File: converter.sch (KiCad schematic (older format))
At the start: 15 parts

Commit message: Schematic mostly complete
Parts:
- removed U?: MSP430G2553-20, ~, symbol MSP430G2553-20
- added C? (x3): CP1, ~, symbol CP1
- added C? (x4): C, ~, symbol C
- added D? (x2): DIODE, ~, symbol DIODE
- added J?: USB-FOO, ~, symbol USB-FOO
- added L?: INDUCTOR, ~, symbol INDUCTOR
- added P? (x11): CONN_1, ~, symbol CONN_1
- added Q?: SOMETHING, SOT-23, symbol BSS138
- added Q? (x2): BC817-40, SOT-23, symbol BC817-40
- added R?: 0.47, ~, symbol R
- added R? (x4): R, ~, symbol R
- added R? (x2): 22, ~, symbol R
- added U?: LT1117-5.0, LLC-20, symbol LM117E
- added U?: MCP6002, symbol MCP6002
- added U?: ATMEGA8U2, symbol ATMEGA8U2
- added X?: CRYSTAL, ~, symbol CRYSTAL
- L?: value INDUCTOR -> 68µH
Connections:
- net labels added: FB_Back, PWM_Back, onewire, xtal1, xtal2
- wire segments 33 -> 108
- no-connect marks 0 -> 1
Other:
- note added: "Back light (3W red)"
- note added: "Front light (15W white)\n"
- note added: "Logic power supply"
- moved on the sheet: C?, D?, L?, P?, R?, U?, U?A

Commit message: First draft PCB layout
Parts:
- removed C?: CP1, ~, symbol CP1
- added C12: 1µ, ~, symbol C
- added C6: 100n, ~, symbol C
- added P7: 12V+, ~, symbol CONN_1
- added P8: 12V-, ~, symbol CONN_1
- added R?: 47k, ~, symbol R
- C1: renamed from C?; value C -> 100n
- C2, C8: renamed from C?; value CP1 -> 100µ
- C3, C5: renamed from C?; value C -> 22p
- C4: renamed from C?; value C -> 1µ
- C7: renamed from C?; value CP1 -> 470µ
- C9: renamed from C?; value CP1 -> 47µ
- D1: renamed from D?; value DIODE -> 1N4148
- P1: renamed from P?; value CONN_1 -> OW1_5V
- P10: renamed from P?; value CONN_1 -> OW3
- P11: renamed from P?; value CONN_1 -> OW3_GND
- P12: renamed from P?; value CONN_1 -> Front+
- P13: renamed from P?; value CONN_1 -> Back+
- P14: renamed from P?; value CONN_1 -> Front-
- P15: renamed from P?; value CONN_1 -> Back-
- P2: renamed from P?; value CONN_1 -> OW1
- P3: renamed from P?; value CONN_1 -> OW1_GND
- P4: renamed from P?; value CONN_1 -> OW2_5V
- P5: renamed from P?; value CONN_1 -> OW2
- P6: renamed from P?; value CONN_1 -> OW2_GND
- P9: renamed from P?; value CONN_1 -> OW3_5V
- R3: renamed from R?; value R -> 4k7
- X1: renamed from X?; value CRYSTAL -> 16MHz
- gave numbers to parts that had none: 24
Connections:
- net labels added: back_neg, back_pos, front_neg, front_pos
- wire segments 108 -> 138

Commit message: Improved ground routing, fixed one error
The error was a missing VCC connection at the back converter's input
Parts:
- removed U2: LT1117-5.0, LLC-20, symbol LM117E
- added U?: LM1117E, LLC-20, symbol LM1117E
- gave numbers to parts that had none: 1
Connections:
- wire segments 138 -> 117
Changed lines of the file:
@@
 LIBS:c_locc-ctrl-cache
 LIBS:usb-mods
+LIBS:lm1117e
 LIBS:converter-cache
 EELAYER 27 0
@@
 Sheet 1 1
 Title ""
-Date "18 oct 2013"
+Date "19 oct 2013"
 Rev ""
 Comp ""
@@
 Text Label 5100 3650 0    60   ~ 0
 PWM_Back
-$Comp
-L LM117E U2
-U 1 1 525F0E52
-P 4150 1100
-F 0 "U2" H 3950 1300 40  0000 C CNN
-F 1 "LT1117-5.0" H 4150 1300 40  0000 L CNN
-F 2 "LLC-20" H 4150 1200 30  0000 C CIN
-F 3 "~" H 4150 1100 60  0000 C CNN
-	1    4150 1100
-	1    0    0    -1
-$EndComp
 $Comp
 L CP1 C2
@@
 	7800 2700 7800 2450
 Wire Wire Line
-	7100 1800 7200 1800
-Wire Wire Line
-	7200 1800 7300 1800
-Wire Wire Line
-	7700 1800 7800 1800
-Wire Wire Line
-	7800 1800 7900 1800
+	7100 1800 7300 1800
+Wire Wire Line
+	7700 1800 7900 1800
 Wire Wire Line
 	7800 2050 7800 1800
@@
 	9300 2100 9350 2100
 Wire Wire Line
-	9850 2200 9900 2200
-Wire Wire Line
-	9900 2200 9950 2200
+	9850 2200 9950 2200
 Connection ~ 9900 2200
 Wire Wire Line
 	10500 2700 10500 2650
 Wire Wire Line
-	10450 2200 10500 2200
-Wire Wire Line
-	10500 2200 10900 2200
+	10450 2200 10900 2200
 Wire Wire Line
 	10500 2200 10500 2250
@@
 Connection ~ 9000 -50
 Wire Wire Line
-	3650 950  3650 1050
-Wire Wire Line
-	3650 1050 3650 1150
+	3650 950  3650 1150
 Wire Wire Line
 	3650 1050 3750 1050
@@
 	4550 1050 4650 1050
 Wire Wire Line
-	4650 950  4650 1050
-Wire Wire Line
-	4650 1050 4650 1150
+	4650 950  4650 1150
 Connection ~ 4650 1050
 Wire Wire Line
@@
 	9300 3750 9350 3750
 Wire Wire Line
-	9850 3850 9900 3850
-Wire Wire Line
-	9900 3850 9950 3850
+	9850 3850 9950 3850
 Connection ~ 9900 3850
 Wire Wire Line
 	10500 4350 10500 4300
 Wire Wire Line
-	10450 3850 10500 3850
-Wire Wire Line
-	10500 3850 10900 3850
+	10450 3850 10900 3850
 Wire Wire Line
 	10500 3850 10500 3900
@@
 	8650 4150 8750 4150
 Wire Wire Line
-	6300 4150 6350 4150
-Wire Wire Line
-	6350 4150 6750 4150
+	6300 4150 6750 4150
 Wire Wire Line
 	6750 4150 6750 3750
 Connection ~ 6350 4150
 Wire Wire Line
-	5900 3450 6350 3450
-Wire Wire Line
-	6350 3450 6500 3450
+	5900 3450 6500 3450
 Wire Wire Line
 	6350 3750 6350 3450
 Connection ~ 6350 3450
 Wire Wire Line
-	5900 3950 5900 4150
-Wire Wire Line
-	5900 4150 5900 4250
+	5900 3950 5900 4250
 Wire Wire Line
 	5900 3950 6050 3950
@@
 	5900 4750 5900 4650
 Wire Wire Line
-	6900 3450 7000 3450
-Wire Wire Line
-	7000 3450 7100 3450
+	6900 3450 7100 3450
 Wire Wire Line
 	7800 4350 7800 4100
 Wire Wire Line
-	7700 3450 7800 3450
-Wire Wire Line
-	7800 3450 7900 3450
+	7700 3450 7900 3450
 Wire Wire Line
 	7800 3450 7800 3700
@@
 	9300 4200 9350 4200
 Wire Wire Line
-	9300 3950 9300 4150
-Wire Wire Line
-	9300 4150 9300 4200
+	9300 3950 9300 4200
 Wire Wire Line
 	9300 3950 9350 3950
@@
 	9300 2550 9350 2550
 Wire Wire Line
-	9300 2300 9300 2500
-Wire Wire Line
-	9300 2500 9300 2550
+	9300 2300 9300 2550
 Wire Wire Line
 	9300 2300 9350 2300
@@
 	2300 1700 2300 1800
 Wire Wire Line
-	2200 1800 2300 1800
-Wire Wire Line
-	2300 1800 2400 1800
+	2200 1800 2400 1800
 Wire Wire Line
 	4250 3300 4250 3250
@@
 	4200 2700 4600 2700
 Wire Wire Line
-	4550 2900 4550 3000
-Wire Wire Line
-	4550 3000 4550 3100
-Wire Wire Line
-	4550 3100 4550 3300
+	4550 2900 4550 3300
 Wire Wire Line
 	4550 2900 4600 2900
@@
 	3850 3050 3600 3050
 Wire Wire Line
-	3900 4100 3900 4350
-Wire Wire Line
-	3900 4350 3900 4400
+	3900 4100 3900 4400
 Connection ~ 3900 4350
 Wire Wire Line
-	4500 4100 4500 4350
-Wire Wire Line
-	4500 4350 4500 4400
+	4500 4100 4500 4400
 Connection ~ 4500 4350
 Wire Wire Line
@@
 	2300 4700 2300 4600
 Wire Wire Line
-	2250 4600 2300 4600
-Wire Wire Line
-	2300 4600 2350 4600
+	2250 4600 2350 4600
 Connection ~ 2300 1800
 Connection ~ 2300 4600
@@
 	9600 2400 9600 2300
 $Comp
-L R R?
+L R R12
 U 1 1 5261574C
 P 5500 3950
-F 0 "R?" V 5580 3950 40  0000 C CNN
+F 0 "R12" V 5580 3950 40  0000 C CNN
 F 1 "47k" V 5507 3951 40  0000 C CNN
 F 2 "~" V 5430 3950 30  0000 C CNN
@@
 Wire Wire Line
 	5500 4450 5600 4450
+$Comp
+L +12V #PWR037
+U 1 1 526283B4
+P 6350 3450
+F 0 "#PWR037" H 6350 3400 20  0001 C CNN
+F 1 "+12V" H 6350 3550 30  0000 C CNN
+F 2 "" H 6350 3450 60  0000 C CNN
+F 3 "" H 6350 3450 60  0000 C CNN
+	1    6350 3450
+	1    0    0    -1
+$EndComp
+$Comp
+L LM1117E U?
+U 1 1 52628562
+P 4150 1100
+F 0 "U?" H 3950 1300 40  0000 C CNN
+F 1 "LM1117E" H 4150 1300 40  0000 L CNN
+F 2 "LLC-20" H 4150 1200 30  0000 C CIN
+F 3 "~" H 4150 1100 60  0000 C CNN
+	1    4150 1100
+	1    0    0    -1
+$EndComp
 $EndSCHEMATC

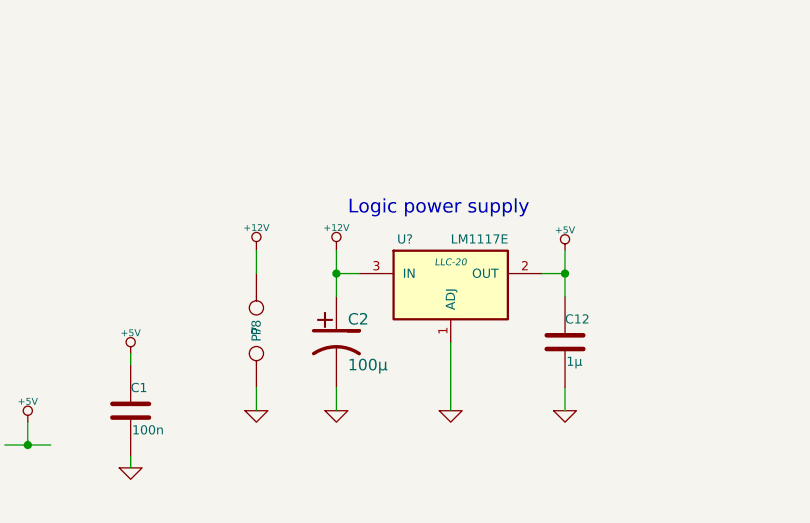
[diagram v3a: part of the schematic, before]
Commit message: Added some info on the back silkscreen
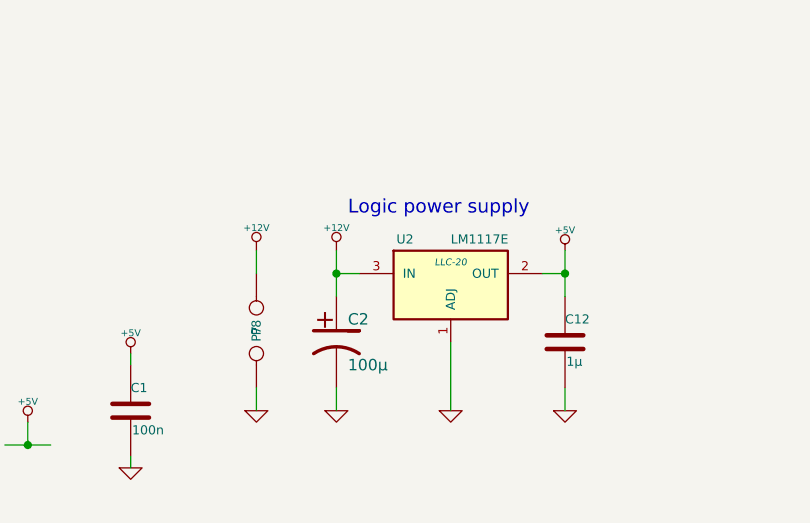
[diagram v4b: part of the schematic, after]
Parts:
- gave numbers to parts that had none: 1
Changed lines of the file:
@@
 $EndComp
 $Comp
-L GND #PWR01
+L GND #PWR29
 U 1 1 525DAC97
 P 7200 2700
-F 0 "#PWR01" H 7200 2700 30  0001 C CNN
+F 0 "#PWR29" H 7200 2700 30  0001 C CNN
 F 1 "GND" H 7200 2630 30  0001 C CNN
 F 2 "" H 7200 2700 60  0000 C CNN
@@
 $EndComp
 $Comp
-L GND #PWR02
+L GND #PWR30
 U 1 1 525DAD46
 P 7800 2700
-F 0 "#PWR02" H 7800 2700 30  0001 C CNN
+F 0 "#PWR30" H 7800 2700 30  0001 C CNN
 F 1 "GND" H 7800 2630 30  0001 C CNN
 F 2 "" H 7800 2700 60  0000 C CNN
@@
 $EndComp
 $Comp
-L GND #PWR03
+L GND #PWR32
 U 1 1 525DADA9
 P 8650 2700
-F 0 "#PWR03" H 8650 2700 30  0001 C CNN
+F 0 "#PWR32" H 8650 2700 30  0001 C CNN
 F 1 "GND" H 8650 2630 30  0001 C CNN
 F 2 "" H 8650 2700 60  0000 C CNN
@@
 PWM_Front
 $Comp
-L GND #PWR04
+L GND #PWR25
 U 1 1 525DAF11
 P 5900 2700
-F 0 "#PWR04" H 5900 2700 30  0001 C CNN
+F 0 "#PWR25" H 5900 2700 30  0001 C CNN
 F 1 "GND" H 5900 2630 30  0001 C CNN
 F 2 "" H 5900 2700 60  0000 C CNN
@@
 $EndComp
 $Comp
-L +12V #PWR05
+L +12V #PWR24
 U 1 1 525DAF47
 P 5900 1800
-F 0 "#PWR05" H 5900 1750 20  0001 C CNN
+F 0 "#PWR24" H 5900 1750 20  0001 C CNN
 F 1 "+12V" H 5900 1900 30  0000 C CNN
 F 2 "" H 5900 1800 60  0000 C CNN
@@
 $EndComp
 $Comp
-L GND #PWR06
+L GND #PWR36
 U 1 1 525DB4F7
 P 10500 2700
-F 0 "#PWR06" H 10500 2700 30  0001 C CNN
+F 0 "#PWR36" H 10500 2700 30  0001 C CNN
 F 1 "GND" H 10500 2630 30  0001 C CNN
 F 2 "" H 10500 2700 60  0000 C CNN
@@
 $EndComp
 $Comp
-L +12V #PWR07
+L +12V #PWR13
 U 1 1 525F0E98
 P 3650 950
-F 0 "#PWR07" H 3650 900 20  0001 C CNN
+F 0 "#PWR13" H 3650 900 20  0001 C CNN
 F 1 "+12V" H 3650 1050 30  0000 C CNN
 F 2 "" H 3650 950 60  0000 C CNN
@@
 $EndComp
 $Comp
-L GND #PWR08
+L GND #PWR14
 U 1 1 525F0FC7
 P 3650 1650
-F 0 "#PWR08" H 3650 1650 30  0001 C CNN
+F 0 "#PWR14" H 3650 1650 30  0001 C CNN
 F 1 "GND" H 3650 1580 30  0001 C CNN
 F 2 "" H 3650 1650 60  0000 C CNN
@@
 $EndComp
 $Comp
-L GND #PWR09
+L GND #PWR23
 U 1 1 525F100B
 P 4650 1650
-F 0 "#PWR09" H 4650 1650 30  0001 C CNN
+F 0 "#PWR23" H 4650 1650 30  0001 C CNN
 F 1 "GND" H 4650 1580 30  0001 C CNN
 F 2 "" H 4650 1650 60  0000 C CNN
@@
 $EndComp
 $Comp
-L GND #PWR010
+L GND #PWR33
 U 1 1 525F131B
 P 8650 4350
-F 0 "#PWR010" H 8650 4350 30  0001 C CNN
+F 0 "#PWR33" H 8650 4350 30  0001 C CNN
 F 1 "GND" H 8650 4280 30  0001 C CNN
 F 2 "" H 8650 4350 60  0000 C CNN
@@
 $EndComp
 $Comp
-L GND #PWR011
+L GND #PWR37
 U 1 1 525F133F
 P 10500 4350
-F 0 "#PWR011" H 10500 4350 30  0001 C CNN
+F 0 "#PWR37" H 10500 4350 30  0001 C CNN
 F 1 "GND" H 10500 4280 30  0001 C CNN
 F 2 "" H 10500 4350 60  0000 C CNN
@@
 $EndComp
 $Comp
-L GND #PWR012
+L GND #PWR26
 U 1 1 525F15F6
 P 5900 4750
-F 0 "#PWR012" H 5900 4750 30  0001 C CNN
+F 0 "#PWR26" H 5900 4750 30  0001 C CNN
 F 1 "GND" H 5900 4680 30  0001 C CNN
 F 2 "" H 5900 4750 60  0000 C CNN
@@
 $EndComp
 $Comp
-L GND #PWR013
+L GND #PWR28
 U 1 1 525F1761
 P 7000 4350
-F 0 "#PWR013" H 7000 4350 30  0001 C CNN
+F 0 "#PWR28" H 7000 4350 30  0001 C CNN
 F 1 "GND" H 7000 4280 30  0001 C CNN
 F 2 "" H 7000 4350 60  0000 C CNN
@@
 $EndComp
 $Comp
-L GND #PWR014
+L GND #PWR31
 U 1 1 525F1767
 P 7800 4350
-F 0 "#PWR014" H 7800 4350 30  0001 C CNN
+F 0 "#PWR31" H 7800 4350 30  0001 C CNN
 F 1 "GND" H 7800 4280 30  0001 C CNN
 F 2 "" H 7800 4350 60  0000 C CNN
@@
 $EndComp
 $Comp
-L GND #PWR015
+L GND #PWR2
 U 1 1 525F21F5
 P 1500 5400
-F 0 "#PWR015" H 1500 5400 30  0001 C CNN
+F 0 "#PWR2" H 1500 5400 30  0001 C CNN
 F 1 "GND" H 1500 5330 30  0001 C CNN
 F 2 "" H 1500 5400 60  0000 C CNN
@@
 $EndComp
 $Comp
-L GND #PWR016
+L GND #PWR6
 U 1 1 525F2338
 P 2300 5400
-F 0 "#PWR016" H 2300 5400 30  0001 C CNN
+F 0 "#PWR6" H 2300 5400 30  0001 C CNN
 F 1 "GND" H 2300 5330 30  0001 C CNN
 F 2 "" H 2300 5400 60  0000 C CNN
@@
 $EndComp
 $Comp
-L GND #PWR017
+L GND #PWR10
 U 1 1 525F235E
 P 3100 5400
-F 0 "#PWR017" H 3100 5400 30  0001 C CNN
+F 0 "#PWR10" H 3100 5400 30  0001 C CNN
 F 1 "GND" H 3100 5330 30  0001 C CNN
 F 2 "" H 3100 5400 60  0000 C CNN
@@
 $EndComp
 $Comp
-L GND #PWR018
+L GND #PWR8
 U 1 1 525DB156
 P 2750 1900
-F 0 "#PWR018" H 2750 1900 30  0001 C CNN
+F 0 "#PWR8" H 2750 1900 30  0001 C CNN
 F 1 "GND" H 2750 1830 30  0001 C CNN
 F 2 "" H 2750 1900 60  0000 C CNN
@@
 $EndComp
 $Comp
-L +5V #PWR019
+L +5V #PWR9
 U 1 1 525F27A2
 P 3100 5100
-F 0 "#PWR019" H 3100 5190 20  0001 C CNN
+F 0 "#PWR9" H 3100 5190 20  0001 C CNN
 F 1 "+5V" H 3100 5190 30  0000 C CNN
 F 2 "" H 3100 5100 60  0000 C CNN
@@
 $EndComp
 $Comp
-L +5V #PWR020
+L +5V #PWR5
 U 1 1 525F27AF
 P 2300 5100
-F 0 "#PWR020" H 2300 5190 20  0001 C CNN
+F 0 "#PWR5" H 2300 5190 20  0001 C CNN
 F 1 "+5V" H 2300 5190 30  0000 C CNN
 F 2 "" H 2300 5100 60  0000 C CNN
@@
 $EndComp
 $Comp
-L +5V #PWR021
+L +5V #PWR1
 U 1 1 525F27B5
 P 1500 5100
-F 0 "#PWR021" H 1500 5190 20  0001 C CNN
+F 0 "#PWR1" H 1500 5190 20  0001 C CNN
 F 1 "+5V" H 1500 5190 30  0000 C CNN
 F 2 "" H 1500 5100 60  0000 C CNN
@@
 $EndComp
 $Comp
-L +5V #PWR022
+L +5V #PWR7
 U 1 1 525F27BB
 P 2750 1400
-F 0 "#PWR022" H 2750 1490 20  0001 C CNN
+F 0 "#PWR7" H 2750 1490 20  0001 C CNN
 F 1 "+5V" H 2750 1490 30  0000 C CNN
 F 2 "" H 2750 1400 60  0000 C CNN
@@
 $EndComp
 $Comp
-L GND #PWR023
+L GND #PWR18
 U 1 1 525F27DA
 P 4150 1650
-F 0 "#PWR023" H 4150 1650 30  0001 C CNN
+F 0 "#PWR18" H 4150 1650 30  0001 C CNN
 F 1 "GND" H 4150 1580 30  0001 C CNN
 F 2 "" H 4150 1650 60  0000 C CNN
@@
 $EndComp
 $Comp
-L +5V #PWR024
+L +5V #PWR22
 U 1 1 525F2842
 P 4650 950
-F 0 "#PWR024" H 4650 1040 20  0001 C CNN
+F 0 "#PWR22" H 4650 1040 20  0001 C CNN
 F 1 "+5V" H 4650 1040 30  0000 C CNN
 F 2 "" H 4650 950 60  0000 C CNN
@@
 $EndComp
 $Comp
-L +5V #PWR025
+L +5V #PWR3
 U 1 1 525F2848
 P 2300 1700
-F 0 "#PWR025" H 2300 1790 20  0001 C CNN
+F 0 "#PWR3" H 2300 1790 20  0001 C CNN
 F 1 "+5V" H 2300 1790 30  0000 C CNN
 F 2 "" H 2300 1700 60  0000 C CNN
@@
 $EndComp
 $Comp
-L GND #PWR026
+L GND #PWR19
 U 1 1 525F13EC
 P 4250 3300
-F 0 "#PWR026" H 4250 3300 30  0001 C CNN
+F 0 "#PWR19" H 4250 3300 30  0001 C CNN
 F 1 "GND" H 4250 3230 30  0001 C CNN
 F 2 "" H 4250 3300 60  0000 C CNN
@@
 $EndComp
 $Comp
-L GND #PWR027
+L GND #PWR21
 U 1 1 525F16BA
 P 4550 3300
-F 0 "#PWR027" H 4550 3300 30  0001 C CNN
+F 0 "#PWR21" H 4550 3300 30  0001 C CNN
 F 1 "GND" H 4550 3230 30  0001 C CNN
 F 2 "" H 4550 3300 60  0000 C CNN
@@
 $EndComp
 $Comp
-L GND #PWR028
+L GND #PWR17
 U 1 1 525F20CA
 P 3900 4850
-F 0 "#PWR028" H 3900 4850 30  0001 C CNN
+F 0 "#PWR17" H 3900 4850 30  0001 C CNN
 F 1 "GND" H 3900 4780 30  0001 C CNN
 F 2 "" H 3900 4850 60  0000 C CNN
@@
 $EndComp
 $Comp
-L GND #PWR029
+L GND #PWR20
 U 1 1 525F2180
 P 4500 4850
-F 0 "#PWR029" H 4500 4850 30  0001 C CNN
+F 0 "#PWR20" H 4500 4850 30  0001 C CNN
 F 1 "GND" H 4500 4780 30  0001 C CNN
 F 2 "" H 4500 4850 60  0000 C CNN
@@
 $EndComp
 $Comp
-L GND #PWR030
+L GND #PWR4
 U 1 1 525F2B7D
 P 2300 4700
-F 0 "#PWR030" H 2300 4700 30  0001 C CNN
+F 0 "#PWR4" H 2300 4700 30  0001 C CNN
 F 1 "GND" H 2300 4630 30  0001 C CNN
 F 2 "" H 2300 4700 60  0000 C CNN
@@
 $EndComp
 $Comp
-L GND #PWR031
+L GND #PWR12
 U 1 1 52614101
 P 3300 1650
-F 0 "#PWR031" H 3300 1650 30  0001 C CNN
+F 0 "#PWR12" H 3300 1650 30  0001 C CNN
 F 1 "GND" H 3300 1580 30  0001 C CNN
 F 2 "" H 3300 1650 60  0000 C CNN
@@
 $EndComp
 $Comp
-L +12V #PWR032
+L +12V #PWR11
 U 1 1 52614111
 P 3300 950
-F 0 "#PWR032" H 3300 900 20  0001 C CNN
+F 0 "#PWR11" H 3300 900 20  0001 C CNN
 F 1 "+12V" H 3300 1050 30  0000 C CNN
 F 2 "" H 3300 950 60  0000 C CNN
@@
 $EndComp
 $Comp
-L GND #PWR033
+L GND #PWR16
 U 1 1 52614580
 P 3650 5500
-F 0 "#PWR033" H 3650 5500 30  0001 C CNN
+F 0 "#PWR16" H 3650 5500 30  0001 C CNN
 F 1 "GND" H 3650 5430 30  0001 C CNN
 F 2 "" H 3650 5500 60  0000 C CNN
@@
 $EndComp
 $Comp
-L +5V #PWR034
+L +5V #PWR15
 U 1 1 52614586
 P 3650 5000
-F 0 "#PWR034" H 3650 5090 20  0001 C CNN
+F 0 "#PWR15" H 3650 5090 20  0001 C CNN
 F 1 "+5V" H 3650 5090 30  0000 C CNN
 F 2 "" H 3650 5000 60  0000 C CNN
@@
 	9600 2100 9600 1950
 $Comp
-L +5V #PWR035
+L +5V #PWR34
 U 1 1 52615406
 P 9600 1950
-F 0 "#PWR035" H 9600 2040 20  0001 C CNN
+F 0 "#PWR34" H 9600 2040 20  0001 C CNN
 F 1 "+5V" H 9600 2040 30  0000 C CNN
 F 2 "" H 9600 1950 60  0000 C CNN
@@
 $EndComp
 $Comp
-L GND #PWR036
+L GND #PWR35
 U 1 1 52615415
 P 9600 2400
-F 0 "#PWR036" H 9600 2400 30  0001 C CNN
+F 0 "#PWR35" H 9600 2400 30  0001 C CNN
 F 1 "GND" H 9600 2330 30  0001 C CNN
 F 2 "" H 9600 2400 60  0000 C CNN
@@
 	5500 4450 5600 4450
 $Comp
-L +12V #PWR037
+L +12V #PWR27
 U 1 1 526283B4
 P 6350 3450
-F 0 "#PWR037" H 6350 3400 20  0001 C CNN
+F 0 "#PWR27" H 6350 3400 20  0001 C CNN
 F 1 "+12V" H 6350 3550 30  0000 C CNN
 F 2 "" H 6350 3450 60  0000 C CNN
@@
 $EndComp
 $Comp
-L LM1117E U?
+L LM1117E U2
 U 1 1 52628562
 P 4150 1100
-F 0 "U?" H 3950 1300 40  0000 C CNN
+F 0 "U2" H 3950 1300 40  0000 C CNN
 F 1 "LM1117E" H 4150 1300 40  0000 L CNN
 F 2 "LLC-20" H 4150 1200 30  0000 C CIN
